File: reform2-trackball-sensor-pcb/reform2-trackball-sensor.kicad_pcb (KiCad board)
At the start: 2 copper layers, 23.8 x 17.8 mm, 10 parts, among them J1 Conn_01x06_Male, U1 PAT9125EL

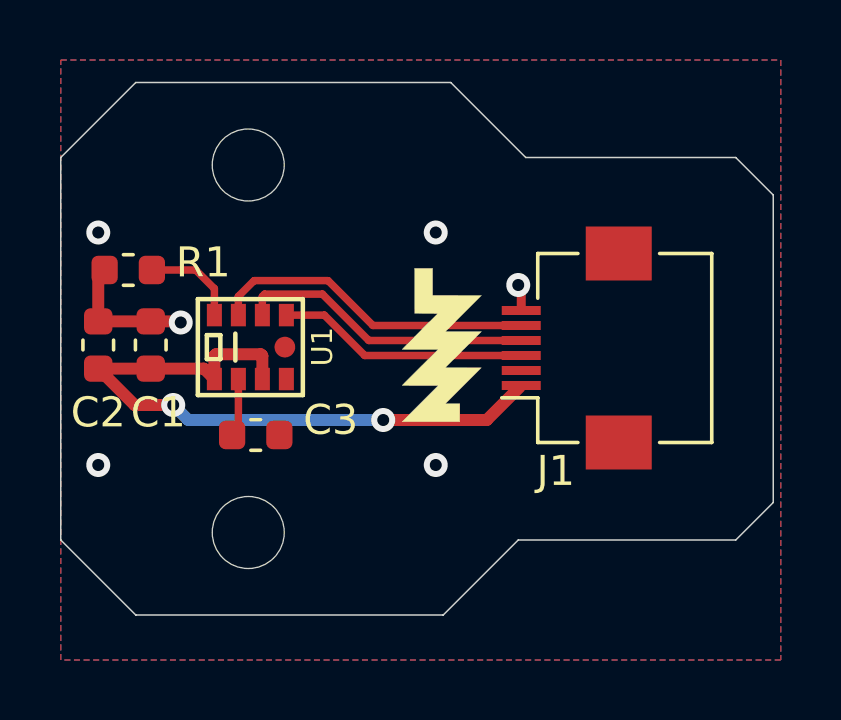
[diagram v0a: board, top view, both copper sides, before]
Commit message: Hardware changes for the mouse-trak
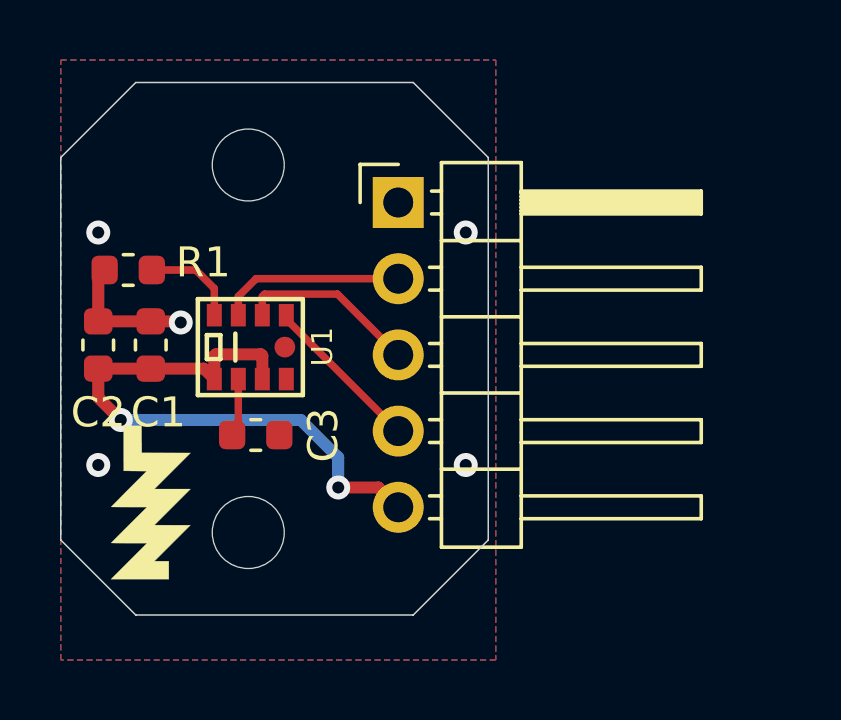
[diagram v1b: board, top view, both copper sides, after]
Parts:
- J1: value Conn_01x06_Male -> Conn_01x05_Male; footprint Connector_FFC-FPC:Hirose_FH12-6S-0.5SH_1x06-1MP_P0.50mm_Horizontal -> Connector_PinHeader_2.54mm:PinHeader_1x05_P2.54mm_Horizontal
- moved H8 16.6 mm to (146.0, 86.0)
- moved H7 11.0 mm to (146.5, 86.8)
- moved J1 7.68 mm to (154.8, 76.8), turned to 0 degrees
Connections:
- J1 pad 1: +3V3 -> GND
- J1 pad 2: Net-(J1-Pad2) -> /MOTION
- J1 pad 3: /SCL -> /SDA
- J1 pad 4: /SDA -> /SCL
- J1 pad 5: /MOTION -> +3V3
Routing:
- net /MOTION: track 10.9 -> 6.20 mm
- net /SDA: track 9.93 -> 6.02 mm
- net /SCL: track 8.39 -> 5.41 mm
- net +3V3: track 22.6 -> 20.3 mm
- net GND: track 5.46 -> 4.57 mm, vias 6 -> 5
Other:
- board size 23.8 x 17.8 mm -> 14.2 x 17.8 mm
